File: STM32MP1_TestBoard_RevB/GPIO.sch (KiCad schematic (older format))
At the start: 13 parts, among them J1 Conn_01x27, J2 Conn_01x27, J3 Conn_01x27, J4 Conn_01x27, J5 Conn_02x03_Odd_Even, J7 Conn_01x08, U1 STM32MP157xAB

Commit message: Updated design
- Added Crystal/Oscillators
- Replaced both SDMMC with single SDMMC w/ detect pin
- Added USB Type C for VIN
- Moved SWD pins
- Tidied up silk screen for pin headers J1, J2, J3, J4
- Moved DSI socket
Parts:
- added C11, C16: 10pF NP0, Capacitor_SMD:C_0402_1005Metric_Pad0.74x0.62mm_HandSolder, symbol Device:C
- added C37: 10nF, Capacitor_SMD:C_0402_1005Metric_Pad0.74x0.62mm_HandSolder, symbol Device:C
- added NT2, NT3: Net-Tie_2, TinyNetTies:NetTie-2_SMD_Pad0.127mm, symbol Device:Net-Tie_2
- added R20: 10R, Resistor_SMD:R_0402_1005Metric_Pad0.72x0.64mm_HandSolder, symbol Device:R
- added R21: 10K, Resistor_SMD:R_0402_1005Metric_Pad0.72x0.64mm_HandSolder, symbol Device:R
- added R22: 1K, Resistor_SMD:R_0402_1005Metric_Pad0.72x0.64mm_HandSolder, symbol Device:R
- added R23: 0R, Resistor_SMD:R_0402_1005Metric_Pad0.72x0.64mm_HandSolder, symbol Device:R
- added X1: ASE-xxxMHz, Oscillator:Oscillator_SMD_Abracon_ASE-4Pin_3.2x2.5mm, symbol Oscillator:ASE-xxxMHz
- added Y1: Crystal, Crystal:Crystal_SMD_2012-2Pin_2.0x1.2mm_HandSoldering, symbol Device:Crystal
- D1: LCSC (none) -> C84256
- R1, R5, R7, R9: LCSC (none) -> C11702
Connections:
- net 3.3V_VDD: now also R20.1
- net GNDS: now also NT2.1, NT3.1
- net PC14: now also C11.2, Y1.1; no longer J3.14 (Pin_14)
- net PC15: now also R23.1; no longer J2.14 (Pin_14)
- net PH1: now also R22.1
- net PH0 renamed HSE_IN
- net HSE_IN: now also X1.3 (OUT)
- new net: C16.2, R23.2, Y1.2
- new net: R21.2, X1.1 (EN)
- new net: C37.2, R20.2, X1.4 (Vdd)
- new net MPU_PWR_ON: R21.1
- new net OSC_GND: C37.1, NT3.2, R22.2, X1.2 (GND)
- new net XTAL_GND: C11.1, C16.1, NT2.2
- no-connect marks 3 -> 5
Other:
- note added: "Connect to \nHSE/LSE\nguard ring.\nonly"
- note added: "uSD_DETECT"

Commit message: completed revb layout
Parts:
- C11, C16: value 10pF NP0 -> 6.8pF NP0; LCSC C1785 -> C1576
- R23: LCSC C25077 -> C25087
- X1: value ASE-xxxMHz -> NX2016SA-24M
- Y1: value Crystal -> NX2012SA32768K1; Mfr NDK -> ECS; Mouser 344-NX2012SA32768K1 -> 520-.327-12.5-12R-T; PartNo NX2012SA-32.768K-STD-MUB-1 -> ECS-.327-12.5-12R-TR
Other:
- moved on the sheet: R21
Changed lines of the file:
@@
 F 5 "~" H 4100 9425 50  0001 C CNN "PartNo"
 F 6 "~" H 4100 9425 50  0001 C CNN "LCSC"
+F 7 "~" H 4100 9425 50  0001 C CNN "Comment"
+F 8 "~" H 4100 9425 50  0001 C CNN "Mouser"
 	1    4100 9425
 	1    0    0    -1
@@
 F 5 "~" H 3475 9050 50  0001 C CNN "PartNo"
 F 6 "C11702" H 3475 9050 50  0001 C CNN "LCSC"
+F 7 "~" H 3475 9050 50  0001 C CNN "Comment"
+F 8 "~" H 3475 9050 50  0001 C CNN "Mouser"
 	1    3475 9050
 	-1   0    0    1
@@
 F 5 "~" H 3175 9050 50  0001 C CNN "PartNo"
 F 6 "C11702" H 3175 9050 50  0001 C CNN "LCSC"
+F 7 "~" H 3175 9050 50  0001 C CNN "Comment"
+F 8 "~" H 3175 9050 50  0001 C CNN "Mouser"
 	1    3175 9050
 	-1   0    0    1
@@
 F 5 "~" H 2875 9050 50  0001 C CNN "PartNo"
 F 6 "C11702" H 2875 9050 50  0001 C CNN "LCSC"
+F 7 "~" H 2875 9050 50  0001 C CNN "Comment"
+F 8 "~" H 2875 9050 50  0001 C CNN "Mouser"
 	1    2875 9050
 	-1   0    0    1
@@
 F 5 "~" H 7375 5625 50  0001 C CNN "PartNo"
 F 6 "~" H 7375 5625 50  0001 C CNN "LCSC"
+F 7 "~" H 7375 5625 50  0001 C CNN "Comment"
+F 8 "~" H 7375 5625 50  0001 C CNN "Mouser"
 	1    7375 5625
 	-1   0    0    1
@@
 F 5 "~" H 9400 10425 50  0001 C CNN "PartNo"
 F 6 "C84256" H 9400 10425 50  0001 C CNN "LCSC"
+F 7 "~" H 9400 10425 50  0001 C CNN "Comment"
+F 8 "~" H 9400 10425 50  0001 C CNN "Mouser"
 	1    9400 10425
 	0    -1   -1   0
@@
 F 5 "~" H 9000 10750 50  0001 C CNN "PartNo"
 F 6 "C11702" H 9000 10750 50  0001 C CNN "LCSC"
+F 7 "~" H 9000 10750 50  0001 C CNN "Comment"
+F 8 "~" H 9000 10750 50  0001 C CNN "Mouser"
 	1    9000 10750
 	0    -1   -1   0
@@
 F 5 "~" H 8900 8225 50  0001 C CNN "PartNo"
 F 6 "~" H 8900 8225 50  0001 C CNN "LCSC"
+F 7 "~" H 8900 8225 50  0001 C CNN "Comment"
+F 8 "~" H 8900 8225 50  0001 C CNN "Mouser"
 	2    8900 8225
 	1    0    0    -1
@@
 F 5 "~" H 8875 3300 50  0001 C CNN "PartNo"
 F 6 "~" H 8875 3300 50  0001 C CNN "LCSC"
+F 7 "~" H 8875 3300 50  0001 C CNN "Comment"
+F 8 "~" H 8875 3300 50  0001 C CNN "Mouser"
 	1    8875 3300
 	1    0    0    -1
@@
 F 5 "~" H 15775 2800 50  0001 C CNN "PartNo"
 F 6 "~" H 15775 2800 50  0001 C CNN "LCSC"
+F 7 "~" H 15775 2800 50  0001 C CNN "Comment"
+F 8 "~" H 15775 2800 50  0001 C CNN "Mouser"
 	1    15775 2800
 	1    0    0    -1
@@
 F 5 "~" H 19775 2800 50  0001 C CNN "PartNo"
 F 6 "~" H 19775 2800 50  0001 C CNN "LCSC"
+F 7 "~" H 19775 2800 50  0001 C CNN "Comment"
+F 8 "~" H 19775 2800 50  0001 C CNN "Mouser"
 	1    19775 2800
 	1    0    0    -1
@@
 F 5 "~" H 19775 6500 50  0001 C CNN "PartNo"
 F 6 "~" H 19775 6500 50  0001 C CNN "LCSC"
+F 7 "~" H 19775 6500 50  0001 C CNN "Comment"
+F 8 "~" H 19775 6500 50  0001 C CNN "Mouser"
 	1    19775 6500
 	1    0    0    -1
@@
 F 5 "~" H 15775 6500 50  0001 C CNN "PartNo"
 F 6 "~" H 15775 6500 50  0001 C CNN "LCSC"
+F 7 "~" H 15775 6500 50  0001 C CNN "Comment"
+F 8 "~" H 15775 6500 50  0001 C CNN "Mouser"
 	1    15775 6500
 	1    0    0    -1
@@
 F 5 "~" H 12000 8325 50  0001 C CNN "PartNo"
 F 6 "~" H 12000 8325 50  0001 C CNN "LCSC"
+F 7 "~" H 12000 8325 50  0001 C CNN "Comment"
+F 8 "~" H 12000 8325 50  0001 C CNN "Mouser"
 	1    12000 8325
 	1    0    0    -1
@@
 P 5250 13450
 F 0 "Y1" V 5275 13725 50  0000 C CNN
-F 1 "Crystal" V 5150 13725 50  0000 C CNN
+F 1 "NX2012SA32768K1" V 5150 13900 50  0000 C CNN
 F 2 "Crystal:Crystal_SMD_2012-2Pin_2.0x1.2mm_HandSoldering" H 5250 13450 50  0001 C CNN
-F 3 "https://www.mouser.co.uk/datasheet/2/905/c_NX2012SA-STD-MUB-1_e-1317508.pdf" H 5250 13450 50  0001 C CNN
+F 3 "https://www.mouser.co.uk/datasheet/2/122/ECX-12R-1314062.pdf" H 5250 13450 50  0001 C CNN
 F 4 "32.768KHz NP0 +/-0.25pF 50V" H 5250 13450 50  0001 C CNN "Comment"
-F 5 "344-NX2012SA32768K1" H 5250 13450 50  0001 C CNN "Mouser"
-F 6 "NDK" H 5250 13450 50  0001 C CNN "Mfr"
-F 7 "NX2012SA-32.768K-STD-MUB-1" H 5250 13450 50  0001 C CNN "PartNo"
+F 5 "520-.327-12.5-12R-T " H 5250 13450 50  0001 C CNN "Mouser"
+F 6 "ECS" H 5250 13450 50  0001 C CNN "Mfr"
+F 7 "ECS-.327-12.5-12R-TR " H 5250 13450 50  0001 C CNN "PartNo"
 F 8 "~" H 5250 13450 50  0001 C CNN "LCSC"
 	1    5250 13450
@@
 P 5950 14075
 F 0 "C11" V 5750 14150 50  0000 R CNN
-F 1 "10pF NP0" V 6125 14175 50  0000 R CNN
+F 1 "6.8pF NP0" V 6125 14175 50  0000 R CNN
 F 2 "Capacitor_SMD:C_0402_1005Metric_Pad0.74x0.62mm_HandSolder" H 5988 13925 50  0001 C CNN
 F 3 "~" H 5950 14075 50  0001 C CNN
-F 4 "C1785" H 5950 14075 50  0001 C CNN "LCSC"
+F 4 "C1576" H 5950 14075 50  0001 C CNN "LCSC"
+F 5 "~" H 5950 14075 50  0001 C CNN "Comment"
+F 6 "~" H 5950 14075 50  0001 C CNN "Mfr"
+F 7 "~" H 5950 14075 50  0001 C CNN "Mouser"
+F 8 "~" H 5950 14075 50  0001 C CNN "PartNo"
 	1    5950 14075
 	0    1    1    0
@@
 P 5950 12825
 F 0 "C16" V 5775 12900 50  0000 R CNN
-F 1 "10pF NP0" V 6100 12900 50  0000 R CNN
+F 1 "6.8pF NP0" V 6100 12900 50  0000 R CNN
 F 2 "Capacitor_SMD:C_0402_1005Metric_Pad0.74x0.62mm_HandSolder" H 5988 12675 50  0001 C CNN
 F 3 "~" H 5950 12825 50  0001 C CNN
-F 4 "C1785" H 5950 12825 50  0001 C CNN "LCSC"
+F 4 "C1576" H 5950 12825 50  0001 C CNN "LCSC"
+F 5 "~" H 5950 12825 50  0001 C CNN "Comment"
+F 6 "~" H 5950 12825 50  0001 C CNN "Mfr"
+F 7 "~" H 5950 12825 50  0001 C CNN "Mouser"
+F 8 "~" H 5950 12825 50  0001 C CNN "PartNo"
 	1    5950 12825
 	0    1    1    0
@@
 P 14000 13750
 F 0 "X1" H 14150 14225 50  0000 L CNN
-F 1 "ASE-xxxMHz" H 14125 14125 50  0000 L CNN
+F 1 "NX2016SA-24M" H 14125 14125 50  0000 L CNN
 F 2 "Oscillator:Oscillator_SMD_Abracon_ASE-4Pin_3.2x2.5mm" H 14700 13400 50  0001 C CNN
 F 3 "http://www.abracon.com/Oscillators/ASV.pdf" H 13900 13750 50  0001 C CNN
@@
 F 3 "~" H 13000 12625 50  0001 C CNN
 F 4 "C15195" H 13000 12625 50  0001 C CNN "LCSC"
+F 5 "~" H 13000 12625 50  0001 C CNN "Comment"
+F 6 "~" H 13000 12625 50  0001 C CNN "Mouser"
 	1    13000 12625
 	-1   0    0    1
@@
 F 5 "~" H 12450 12325 50  0001 C CNN "PartNo"
 F 6 "C25077" H 12450 12325 50  0001 C CNN "LCSC"
+F 7 "~" H 12450 12325 50  0001 C CNN "Comment"
+F 8 "~" H 12450 12325 50  0001 C CNN "Mouser"
 	1    12450 12325
 	0    -1   -1   0
@@
 F 5 "~" H 16075 13125 50  0001 C CNN "PartNo"
 F 6 "C11702" H 16075 13125 50  0001 C CNN "LCSC"
+F 7 "~" H 16075 13125 50  0001 C CNN "Comment"
+F 8 "~" H 16075 13125 50  0001 C CNN "Mouser"
 	1    16075 13125
 	1    0    0    -1
@@
 	16075 13275 16075 13850
 Wire Wire Line
-	13700 13750 12975 13750
+	13700 13750 12600 13750
 $Comp
 L Device:R R?
 U 1 1 60B5B7B1
-P 12825 13750
+P 12450 13750
 AR Path="/60B5B7B1" Ref="R?"  Part="1"
 AR Path="/6097C138/60B5B7B1" Ref="R21"  Part="1"
-F 0 "R21" V 12975 13750 50  0000 C CNN
-F 1 "10K" V 12900 13750 50  0000 C CNN
-F 2 "Resistor_SMD:R_0402_1005Metric_Pad0.72x0.64mm_HandSolder" V 12755 13750 50  0001 C CNN
-F 3 "~" H 12825 13750 50  0001 C CNN
-F 4 "~" H 12825 13750 50  0001 C CNN "Mfr"
-F 5 "~" H 12825 13750 50  0001 C CNN "PartNo"
-F 6 "C25744" H 12825 13750 50  0001 C CNN "LCSC"
-	1    12825 13750
+F 0 "R21" V 12600 13750 50  0000 C CNN
+F 1 "10K" V 12525 13750 50  0000 C CNN
+F 2 "Resistor_SMD:R_0402_1005Metric_Pad0.72x0.64mm_HandSolder" V 12380 13750 50  0001 C CNN
+F 3 "~" H 12450 13750 50  0001 C CNN
+F 4 "~" H 12450 13750 50  0001 C CNN "Mfr"
+F 5 "~" H 12450 13750 50  0001 C CNN "PartNo"
+F 6 "C25744" H 12450 13750 50  0001 C CNN "LCSC"
+F 7 "~" H 12450 13750 50  0001 C CNN "Comment"
+F 8 "~" H 12450 13750 50  0001 C CNN "Mouser"
+	1    12450 13750
 	0    -1   -1   0
 $EndComp
 Wire Wire Line
-	12675 13750 11650 13750
+	12300 13750 11650 13750
 Text HLabel 11650 13750 0    50   Input ~ 0
 MPU_PWR_ON
@@
 F 4 "~" H 4625 12825 50  0001 C CNN "Mfr"
 F 5 "~" H 4625 12825 50  0001 C CNN "PartNo"
-F 6 "C25077" H 4625 12825 50  0001 C CNN "LCSC"
+F 6 "C25087" H 4625 12825 50  0001 C CNN "LCSC"
+F 7 "~" H 4625 12825 50  0001 C CNN "Comment"
+F 8 "~" H 4625 12825 50  0001 C CNN "Mouser"
 	1    4625 12825
 	0    -1   -1   0
@@
 F 2 "TinyNetTies:NetTie-2_SMD_Pad0.127mm" H 17825 13125 50  0001 C CNN
 F 3 "~" H 17825 13125 50  0001 C CNN
+F 4 "~" H 17825 13125 50  0001 C CNN "Comment"
+F 5 "~" H 17825 13125 50  0001 C CNN "LCSC"
+F 6 "~" H 17825 13125 50  0001 C CNN "Mfr"
+F 7 "~" H 17825 13125 50  0001 C CNN "Mouser"
+F 8 "~" H 17825 13125 50  0001 C CNN "PartNo"
 	1    17825 13125
 	0    -1   -1   0
@@
 F 2 "TinyNetTies:NetTie-2_SMD_Pad0.127mm" H 8000 13400 50  0001 C CNN
 F 3 "~" H 8000 13400 50  0001 C CNN
+F 4 "~" H 8000 13400 50  0001 C CNN "Comment"
+F 5 "~" H 8000 13400 50  0001 C CNN "LCSC"
+F 6 "~" H 8000 13400 50  0001 C CNN "Mfr"
+F 7 "~" H 8000 13400 50  0001 C CNN "Mouser"
+F 8 "~" H 8000 13400 50  0001 C CNN "PartNo"
 	1    8000 13400
 	0    -1   -1   0

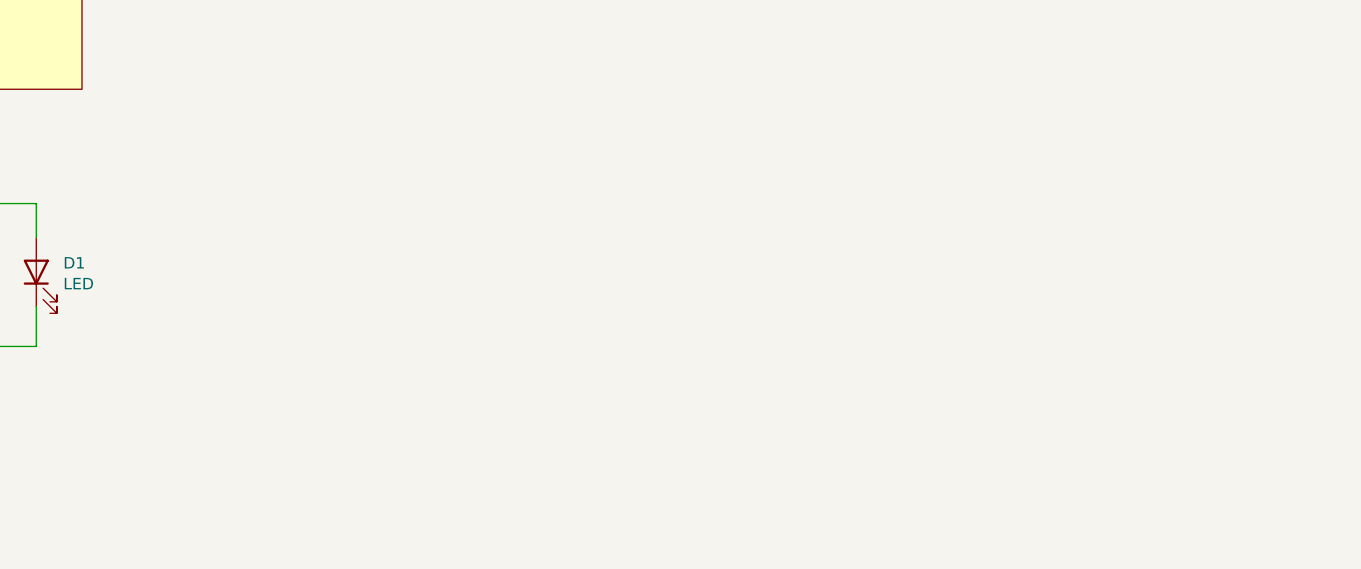
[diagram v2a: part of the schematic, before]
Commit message: fixed BOM error
R4 listed with capacitor part number, corrected to resistor part number
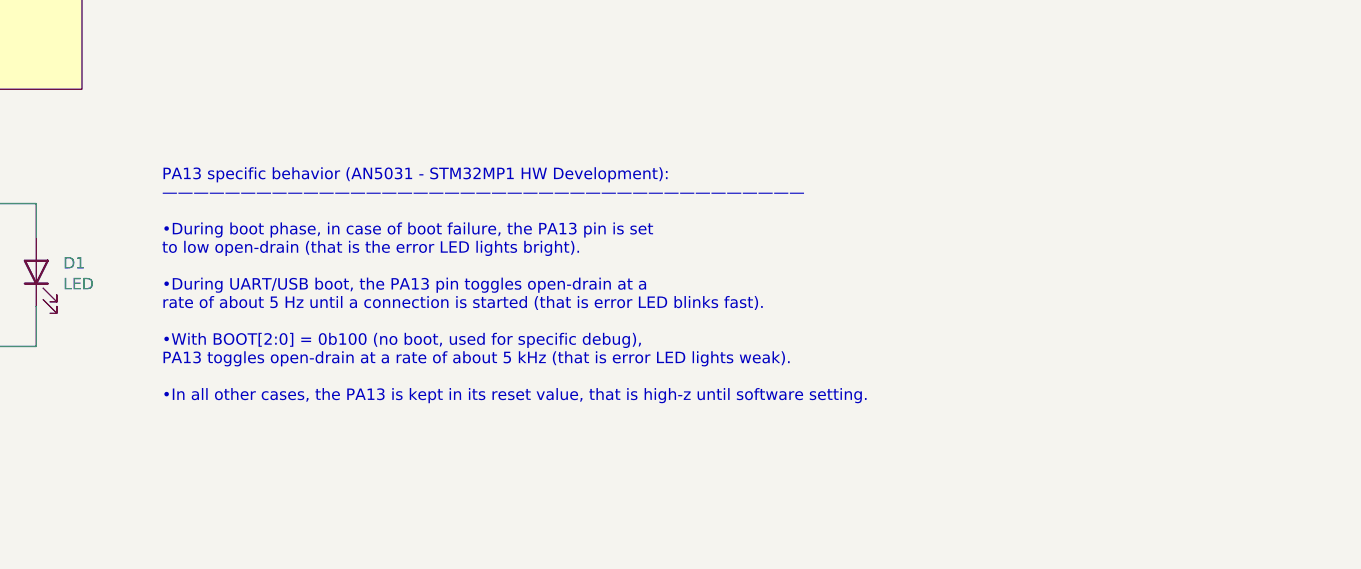
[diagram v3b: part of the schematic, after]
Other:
- note added: "PA13 specific behavior (AN5031 - STM32MP1 HW Development):\n—————————————————————————————————————————\n\n•During boot phase, in case of boot failure, the PA13 pin is set \nto low open-drain (that is the error LED lights bright).\n\n•During UART/USB boot, the PA13 pin toggles open-drain at a \nrate of about 5 Hz until a connection is started (that is error LED blinks fast).\n\n•With BOOT[2:0] = 0b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"
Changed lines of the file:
@@
 Wire Wire Line
 	17825 12825 17825 13025
+Text Notes 9950 11000 0    50   ~ 0
+PA13 specific behavior (AN5031 - STM32MP1 HW Development):\n—————————————————————————————————————————\n\n•During boot phase, in case of boot failure, the PA13 pin is set \nto low open-drain (that is the error LED lights bright).\n\n•During UART/USB boot, the PA13 pin toggles open-drain at a \nrate of about 5 Hz until a connection is started (that is error LED blinks fast).\n\n•With BOOT[2:0] = 0b100 (no boot, used for specific debug), \nPA13 toggles open-drain at a rate of about 5 kHz (that is error LED lights weak). \n\n•In all other cases, the PA13 is kept in its reset value, that is high-z until software setting.
 $EndSCHEMATC
